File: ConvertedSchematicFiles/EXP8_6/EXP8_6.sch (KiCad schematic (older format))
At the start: 9 parts, among them U1 74107, U2 74107, U3 74107

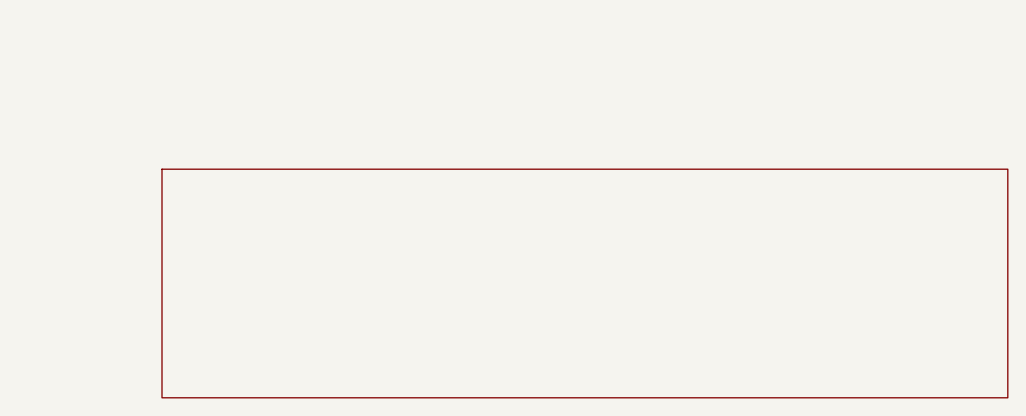
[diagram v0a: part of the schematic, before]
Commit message: Excluded some components. These no longer appear after conversion. When calling shell commands, filenames are in "quotes"
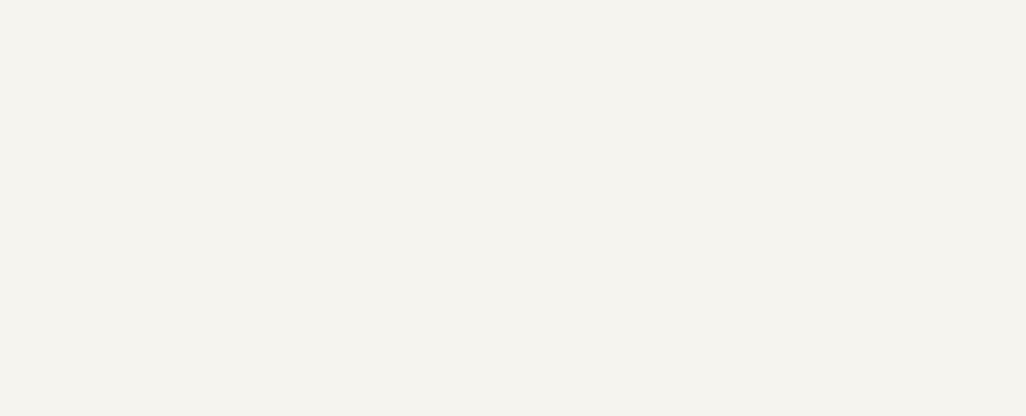
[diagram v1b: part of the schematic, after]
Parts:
- removed titleblk: titleblk, symbol TITLEBLK_PSPICE
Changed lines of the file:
@@
-	1    0    0    1
-$EndComp
-$Comp
-L TITLEBLK_PSPICE titleblk
-U 1 1 66516649
-P 9700 7200
-F 0 "titleblk" H 19400 14400 30  0001 L CNN
-F 1 "titleblk" H 19400 14480 30  0001 L CNN
-	1    9700 7200
 	1    0    0    1
 $EndComp

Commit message: Ports issue fixed. Now annotation for ports is #PWR? function added "itos"
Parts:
- removed EGND (x2): EGND, symbol EGND_PSPICE
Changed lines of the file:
@@
 $EndDescr
 $Comp
-L EGND_PSPICE EGND
+L EGND_PSPICE #PWR1
 U 1 1 14289383
 P 1500 3600
-F 0 "EGND" H 3000 7200 30  0001 L CNN
+F 0 "#PWR1" H 3000 7200 30  0001 L CNN
 F 1 "EGND" H 3000 7280 30  0001 L CNN
 	1    1500 3600
@@
 $EndComp
 $Comp
-L EGND_PSPICE EGND
+L EGND_PSPICE #PWR2
 U 1 1 46930886
 P 4900 4700
-F 0 "EGND" H 9800 9400 30  0001 L CNN
+F 0 "#PWR2" H 9800 9400 30  0001 L CNN
 F 1 "EGND" H 9800 9480 30  0001 L CNN
 	1    4900 4700

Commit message: Added LICENSE.txt
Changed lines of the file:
@@
 $EndDescr
 $Comp
-L EGND_PSPICE #PWR1
+L GND #PWR1
 U 1 1 14289383
 P 1500 3600
@@
 $EndComp
 $Comp
-L EGND_PSPICE #PWR2
+L GND #PWR2
 U 1 1 46930886
 P 4900 4700

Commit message: Orientation fix. Library components are now inverted, with +ve y axis going up. In Schematic files, +ve y axis is downwards. This is how the KiCad libraries are. As a result of the above fixed, the converted GND is now oriented correctly.
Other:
- moved on the sheet: U1, U2, U3, V1, V2
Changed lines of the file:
@@
 F 1 "EGND" H 3000 7280 30  0001 L CNN
 	1    1500 3600
-	1    0    0    1
+	1    0    0    -1
 $EndComp
 $Comp
@@
 F 1 "EGND" H 9800 9480 30  0001 L CNN
 	1    4900 4700
-	1    0    0    1
+	1    0    0    -1
 $EndComp
 $Comp
@@
 F 1 "5V" H 1500 3090 30  0000 C CNN
 	1    1500 3200
-	1    0    0    1
+	1    0    0    -1
 $EndComp
 $Comp
@@
 F 1 "5V" H 4900 4190 30  0000 C CNN
 	1    4900 4300
-	1    0    0    1
+	1    0    0    -1
 $EndComp
 $Comp
@@
 F 1 "DigClock" H 1900 4480 30  0000 L CNN
 	1    1900 4400
-	1    0    0    1
+	1    0    0    -1
 $EndComp
 $Comp
@@
 F 1 "74107" H 2200 3480 30  0000 L CNN
 	1    2200 3400
-	1    0    0    1
+	1    0    0    -1
 $EndComp
 $Comp
@@
 F 1 "74107" H 3300 3480 30  0000 L CNN
 	1    3300 3400
-	1    0    0    1
+	1    0    0    -1
 $EndComp
 $Comp
@@
 F 1 "74107" H 4600 3480 30  0000 L CNN
 	1    4600 3400
-	1    0    0    1
+	1    0    0    -1
 $EndComp
 Wire Wire Line

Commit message: Removed the use of exec, wrote basename function, made integration with eSim easier.
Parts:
- added titleblk: titleblk, symbol titleblk_PSPICE
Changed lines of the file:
@@
-EESchema Schematic File Version 2  date Saturday 04 March 2000 03:24:31 PM IST
+EESchema Schematic File Version 2  date
 LIBS:power
 LIBS:device
@@
 LIBS:contrib
 LIBS:valves
-LIBS:ConvertedSchematicFiles/EXP8_6-cache
 EELAYER 25  0
 EELAYER END
@@
 Sheet 1 1
 Title ""
-Date "04 Mar 2000"
+Date ""
 Rev ""
 Comp ""
@@
 	1    0    0    -1
 $EndComp
+$Comp
+L titleblk_PSPICE titleblk
+U 1 1 66516649
+P 9700 7200
+F 0 "titleblk" H 19400 14400 30  0001 L CNN
+F 1 "titleblk" H 19400 14480 30  0001 L CNN
+	1    9700 7200
+	1    0    0    -1
+$EndComp
